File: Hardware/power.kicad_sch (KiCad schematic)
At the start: 58 parts, among them J1 USB4110GFA, Q1 AO3407A, U1 TPS54302, U13 XC6206PxxxMR, U2 AP63205WU, U3 AP2112K-3.3, U4 USBLC6-2SC6, U6 INA226

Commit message: Added Necessary Connectors, pads and comments in the respective file
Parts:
- renumbered C16 to C10, C17 to C11, C3 to C12, C19 to C13, C23 to C14, C25 to C15, C29 to C16, C8 to C17, C13 to C18, C14 to C19, C4 to C20, C58 to C21, C57 to C22, C10 to C23, C5 to C3, C7 to C4, C6 to C5, C9 to C6, C11 to C7, C12 to C8, C15 to C9, D2 to D1, D1 to D2, D7 to D3, D3 to D5, R13 to R10, R14 to R11, R15 to R12, R17 to R13, R18 to R14, R19 to R15, R7 to R16, R6 to R17, R8 to R6, R9 to R7, R10 to R8, R12 to R9, U4 to U2, U6 to U3, U2 to U4, U3 to U5, U13 to U6
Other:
- note added: "4) TPS54302 is 3A capable Buck, Expected to handle users external modules attachements. DJI Air Unit, Analog VTX, etc..."

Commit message: Added Digital Airspeed Sensor Connector, Changed the Magnetometer
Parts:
- removed C10, C11: 10uF, Capacitor_SMD:C_0603_1608Metric, symbol Device:C_Small
- removed C13: 0.1uF, Capacitor_SMD:C_0603_1608Metric, symbol Device:C_Small
- removed U6: XC6206PxxxMR, Package_TO_SOT_SMD:SOT-23-3, symbol Regulator_Linear:XC6206PxxxMR
- added U6: AP7343-33W5-7, memo:(AP7343 )SOT-25_L3.0-W1.6-P0.95-LS2.8-BL, symbol AP7343:AP7343-33W5-7
- renumbered C12 to C10, C14 to C11, C15 to C12, C16 to C13, C17 to C14, C18 to C15, C19 to C16, C20 to C17, C21 to C18, C23 to C19, C22 to C20
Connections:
- net +3V3_Sensors: now also U6.5 (VOUT)
- net +5V: now also U6.1 (VIN), U6.3 (EN)
- net GND: now also U6.2 (GND)
- no-connect marks 2 -> 3
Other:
- note added: "low noise high PSSR 300mA LDO"
- moved on the sheet: C17, C18, C19, C20, D1, D5, R15, R16, R17, R8, U5

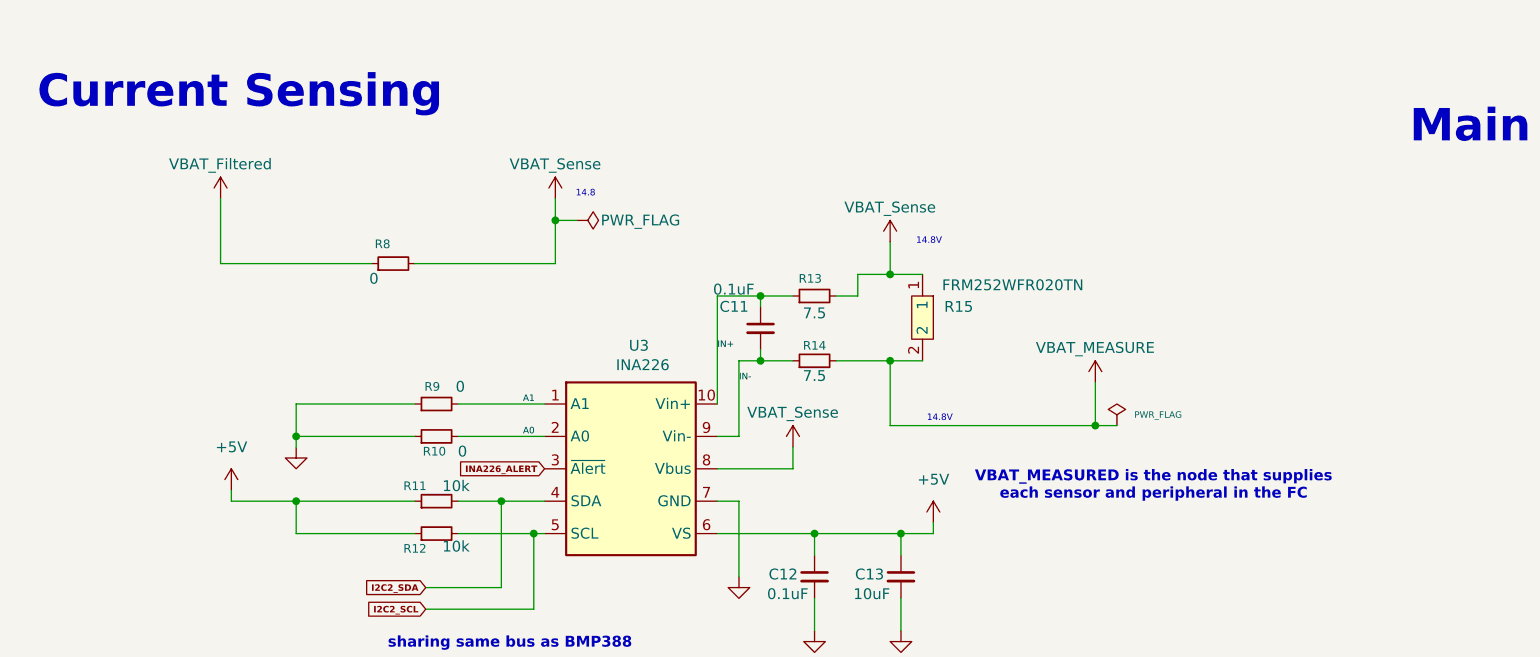
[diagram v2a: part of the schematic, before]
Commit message: clearing unnecessary net classes in power schematics
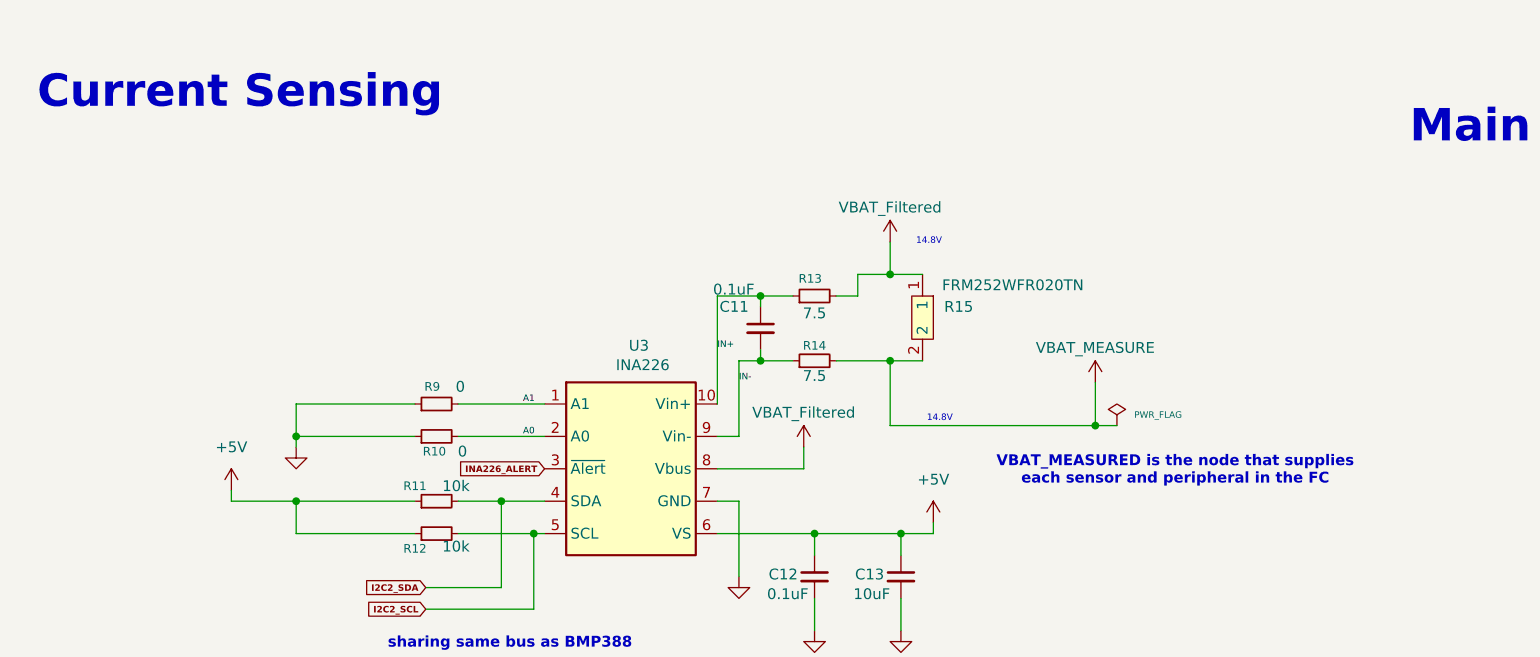
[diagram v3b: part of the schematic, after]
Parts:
- removed R8: 0, Resistor_SMD:R_0402_1005Metric, symbol Device:R_Small
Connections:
- net VBAT_Sense is gone; now on net VBAT_Filtered: R13.2, R15.1, U3.8 (Vbus)
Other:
- note removed: "14.8"

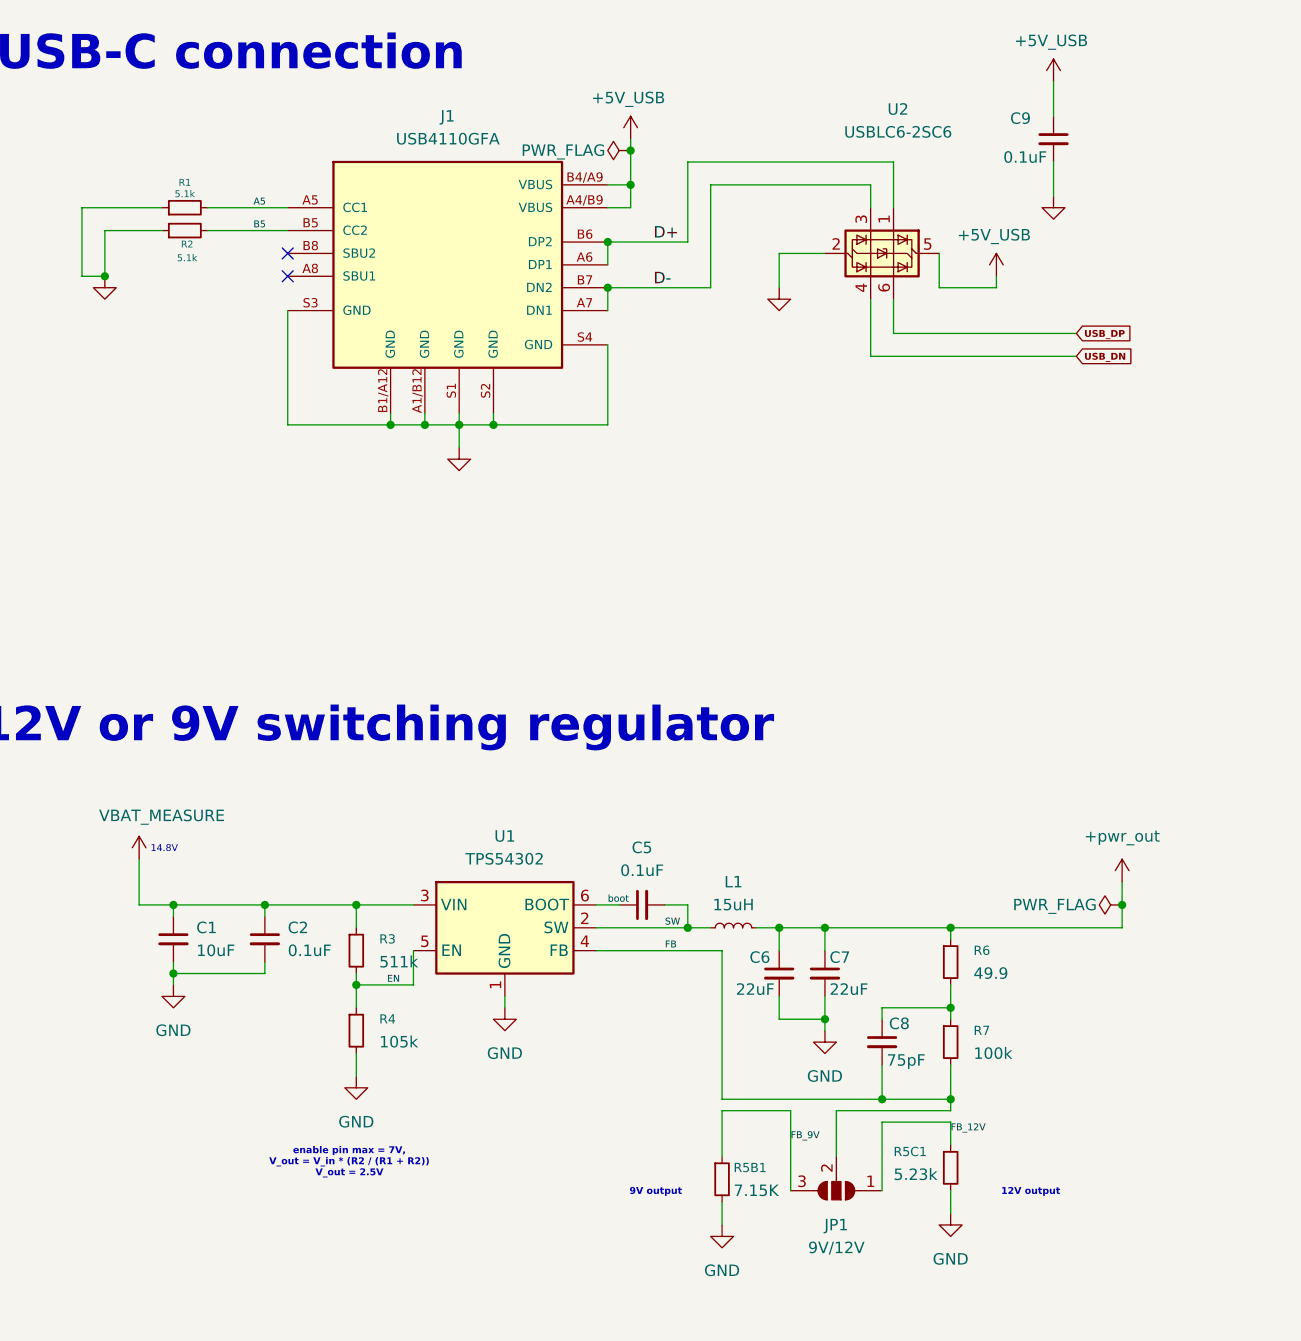
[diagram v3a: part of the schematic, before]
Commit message: removed enable pin resistor in 9V/12V regulator and Layout progress
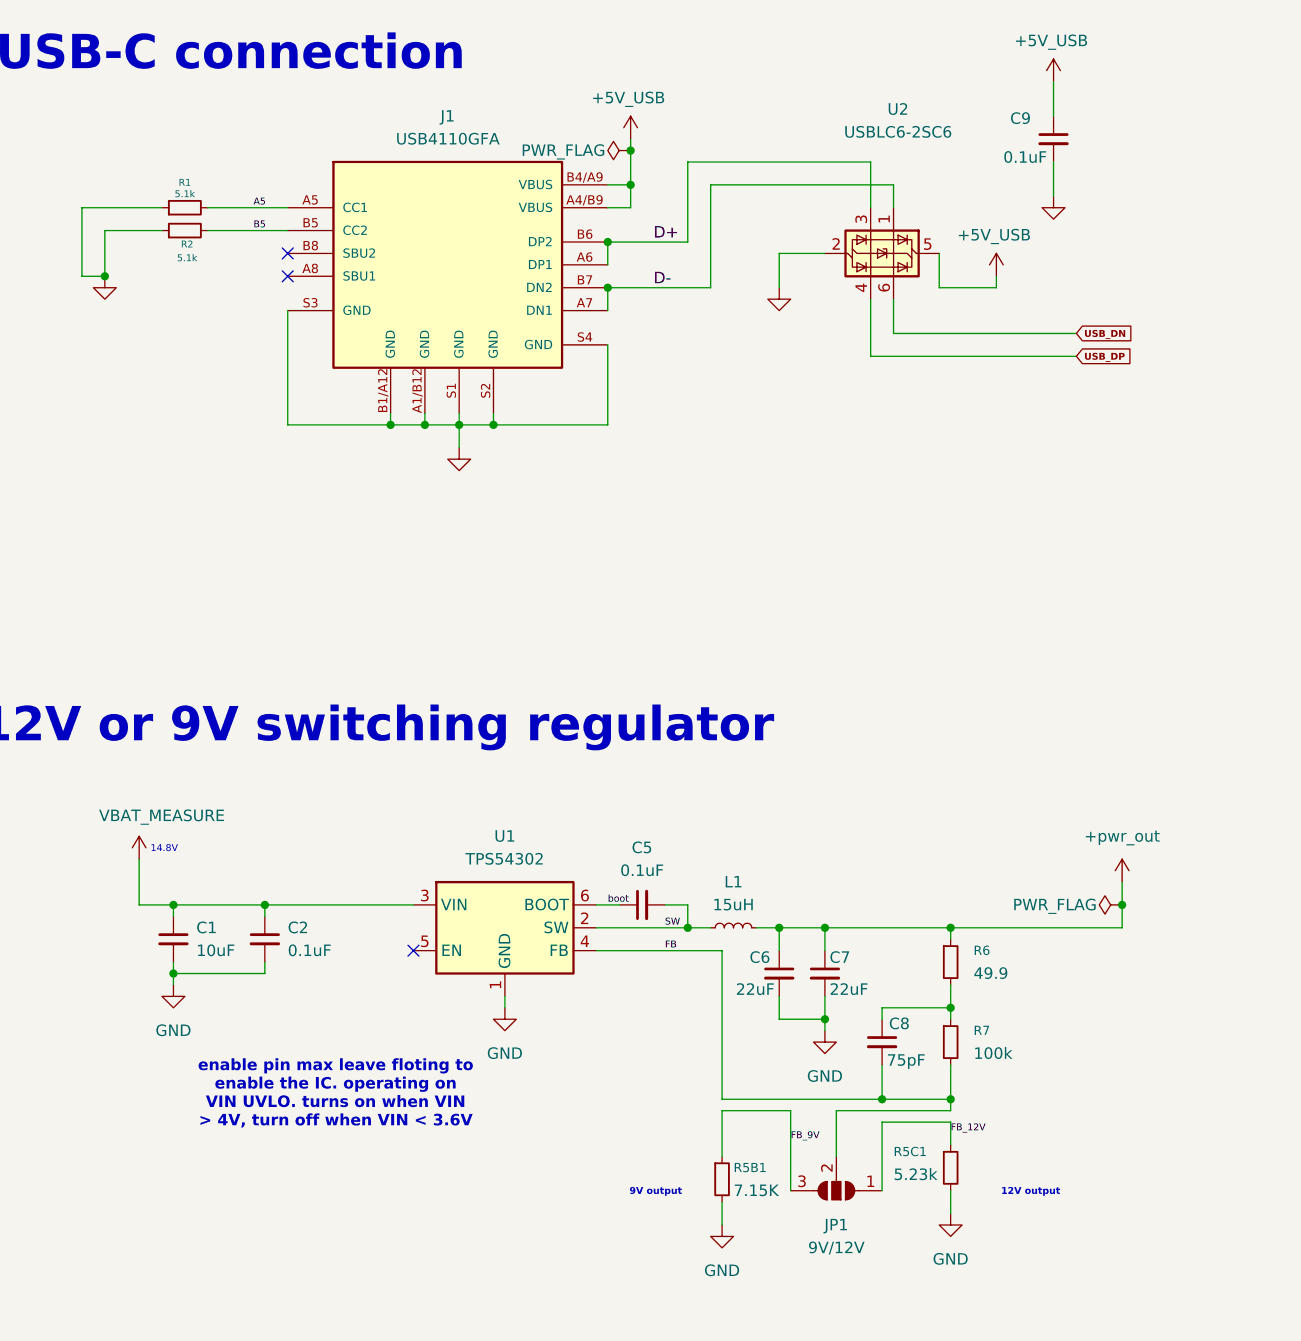
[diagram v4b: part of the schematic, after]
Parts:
- removed R3: 511k, Resistor_SMD:R_0402_1005Metric, symbol Device:R_Small
- removed R4: 105k, Resistor_SMD:R_0402_1005Metric, symbol Device:R_Small
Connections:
- net D+: now also U2.3 (I/O2); no longer U2.1 (I/O1)
- net D-: now also U2.1 (I/O1); no longer U2.3 (I/O2)
- net USB_DN: now also U2.6 (I/O1); no longer U2.4 (I/O2)
- net USB_DP: now also U2.4 (I/O2); no longer U2.6 (I/O1)
- net EN: no longer names the net of U1.5 (EN)
- no-connect marks 3 -> 4
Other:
- note added: "enable pin max leave floting to enable the IC. operating on VIN UVLO. turns on when VIN > 4V, turn off when VIN < 3.6V"
- note removed: "enable pin max = 7V, V_out = V_in * (R2 / (R1 + R2)) V_out = 2.5V"

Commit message: Changed to CMOS, layout progress
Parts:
- renumbered R13 to R10, R14 to R11, R15 to R12, R16 to R13, R17 to R14, R5 to R3, R6 to R4, R7 to R5, R9 to R6, R10 to R7, R11 to R8, R12 to R9

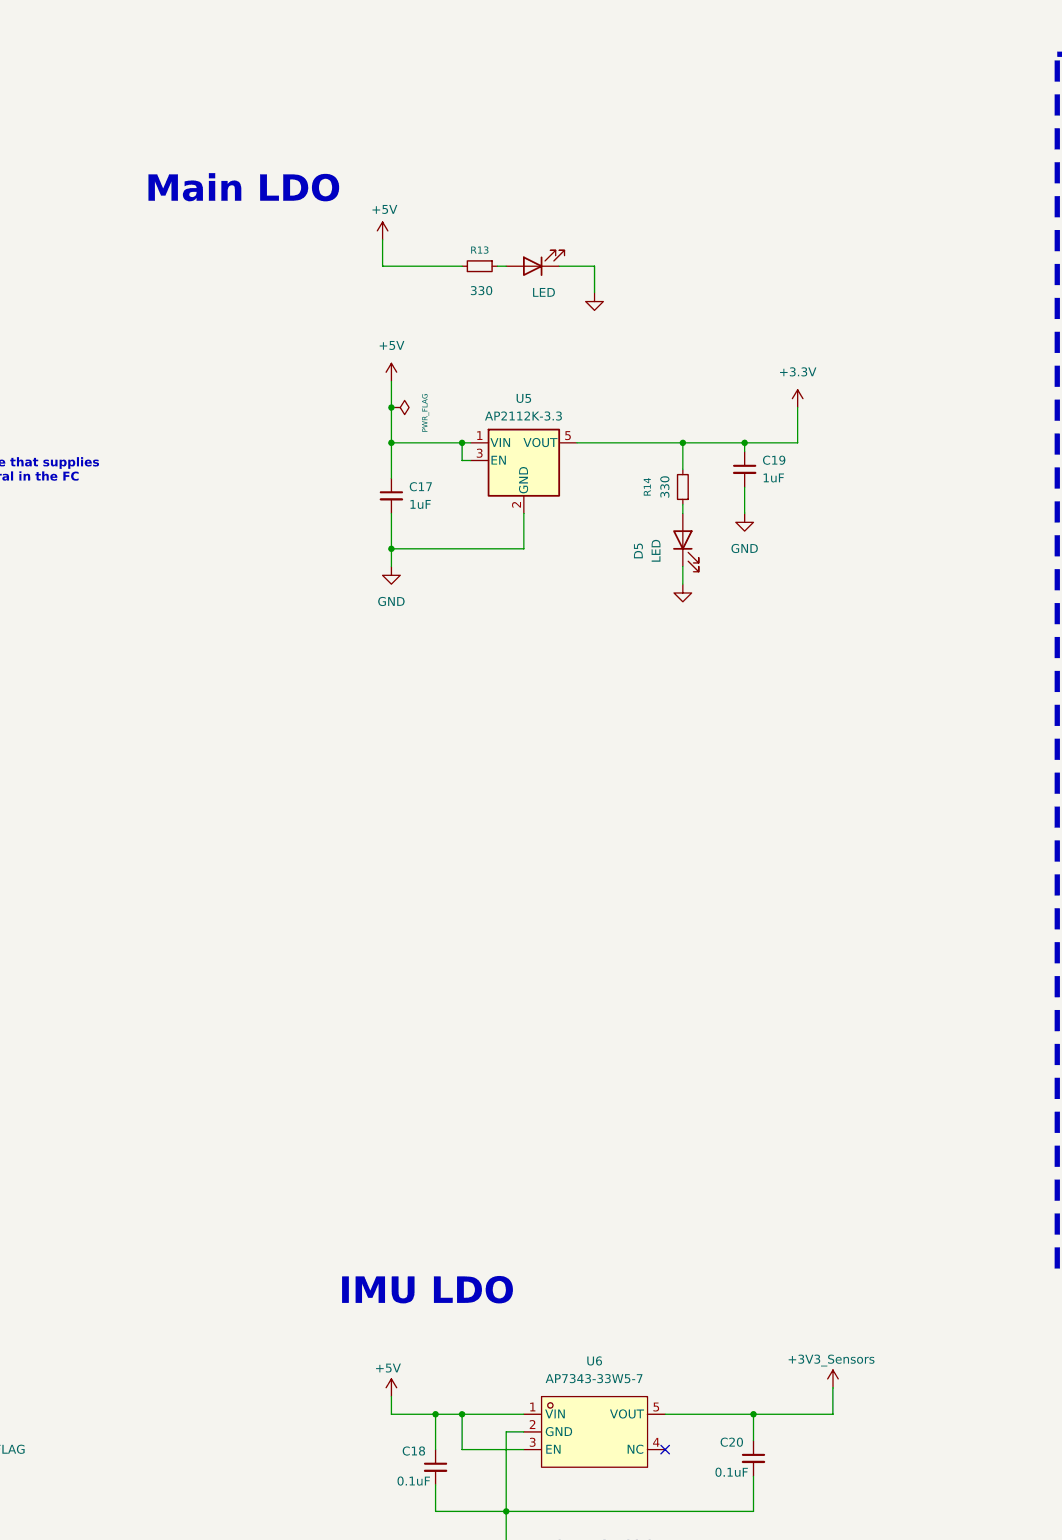
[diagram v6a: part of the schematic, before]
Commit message: added CAN connector
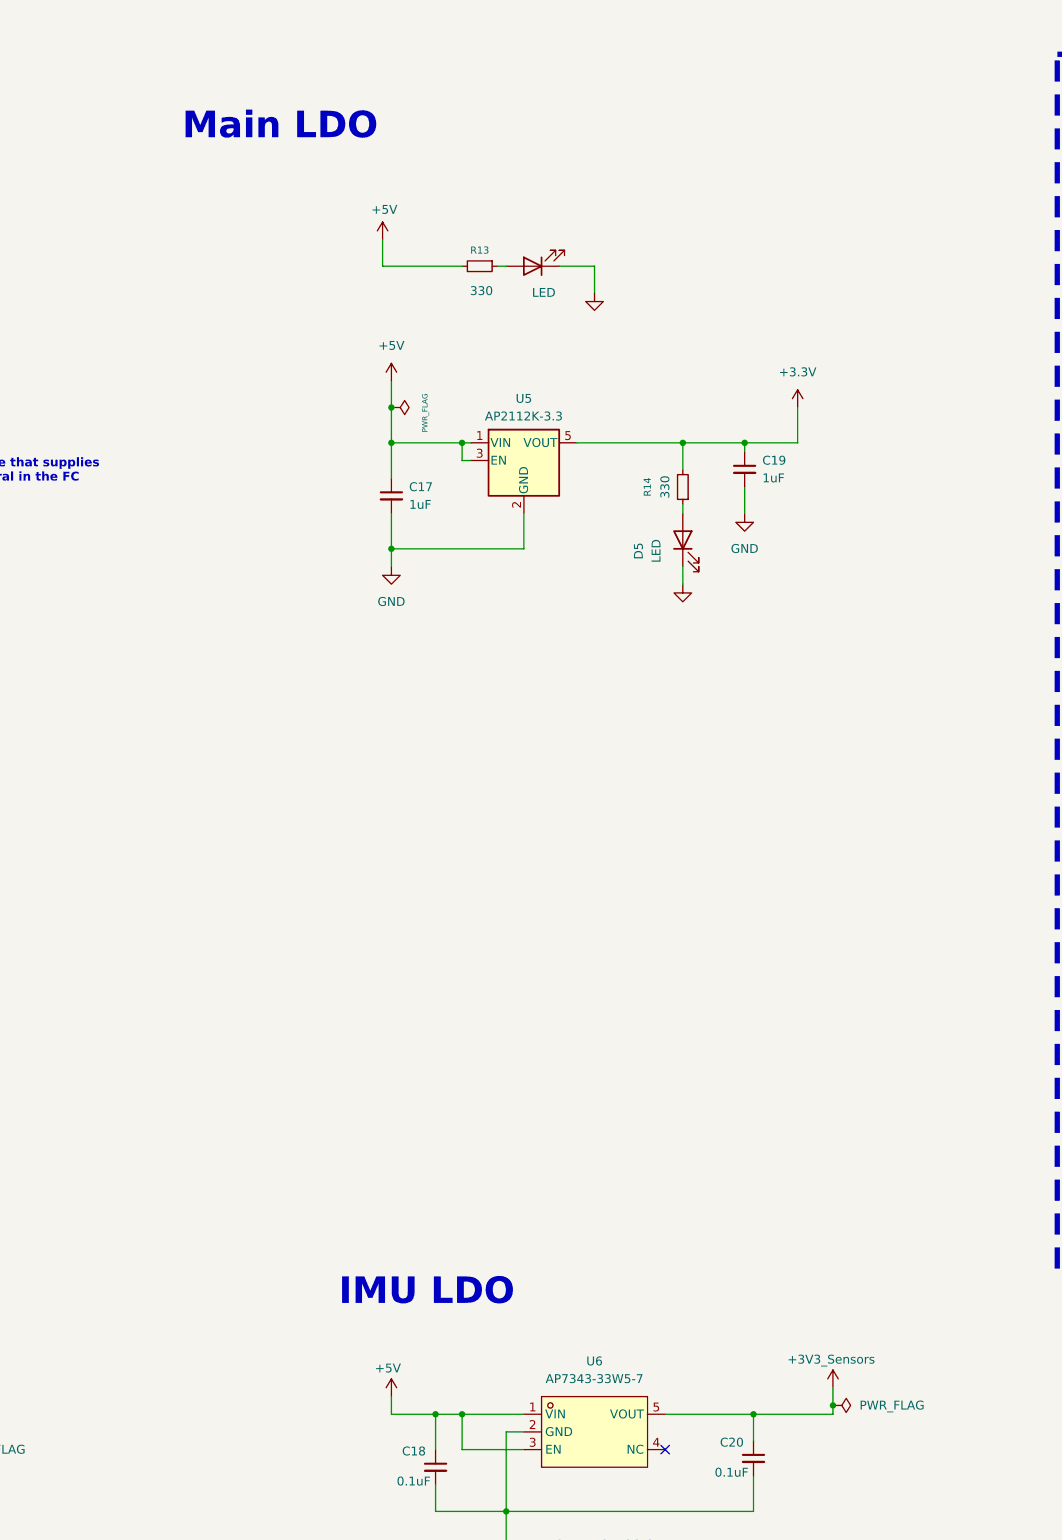
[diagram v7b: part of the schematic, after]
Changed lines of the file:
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@@
 	(text "Main LDO "
 		(exclude_from_sim no)
-		(at 330.454 38.608 0)
+		(at 335.788 29.464 0)
 		(effects
 			(font
@@
 	)
 	(junction
+		(at 415.29 213.36)
+		(diameter 0)
+		(color 0 0 0 0)
+	)
+	(junction
 		(at 87.63 77.47)
 		(diameter 0)
@@
 	(wire
 		(pts
+			(xy 415.29 213.36) (xy 415.29 210.82)
+		)
+		(stroke
+			(width 0)
+			(type default)
+		)
+	)
+	(wire
+		(pts
 			(xy 368.3 217.17) (xy 368.3 228.6)
 		)
@@
 	(wire
 		(pts
-			(xy 415.29 214.63) (xy 415.29 210.82)
+			(xy 415.29 214.63) (xy 415.29 213.36)
 		)
 		(stroke
@@
 					(unit 1)
 				)
+			)
+		)
+	)
+	(symbol
+		(lib_id "power:PWR_FLAG")
+		(at 415.29 213.36 270)
+		(unit 1)
+		(exclude_from_sim no)
+		(in_bom yes)
+		(on_board yes)
+		(dnp no)
+		(fields_autoplaced yes)
+		(property "Reference" "#FLG010"
+			(at 417.195 213.36 0)
+			(effects
+				(font
+					(size 1.27 1.27)
+				)
+				(hide yes)
+			)
+		)
+		(property "Value" "PWR_FLAG"
+			(at 419.1 213.3599 90)
+			(effects
+				(font
+					(size 1.27 1.27)
+				)
+				(justify left)
+			)
+		)
+		(property "Footprint" ""
+			(at 415.29 213.36 0)
+			(effects
+				(font
+					(size 1.27 1.27)
+				)
+				(hide yes)
+			)
+		)
+		(property "Datasheet" "~"
+			(at 415.29 213.36 0)
+			(effects
+				(font
+					(size 1.27 1.27)
+				)
+				(hide yes)
+			)
+		)
+		(property "Description" "Special symbol for telling ERC where power comes from"
+			(at 415.29 213.36 0)
+			(effects
+				(font
+					(size 1.27 1.27)
+				)
+				(hide yes)
+			)
+		)
+		(pin "1"
+		)
+		(instances
+			(project ""
+				(path "/affbaa1c-796a-43e2-b357-d8056264fe45/4a7cbebd-f698-4bee-b98f-1e10a25991ff"
+					(reference "#FLG010")
+					(unit 1)
+				)
